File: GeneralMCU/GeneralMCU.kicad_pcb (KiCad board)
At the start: 2 copper layers, 59 parts, among them J1 ARM_JTAG_SWD, U1 STM32F303R6Tx, U2 SN65HVD230

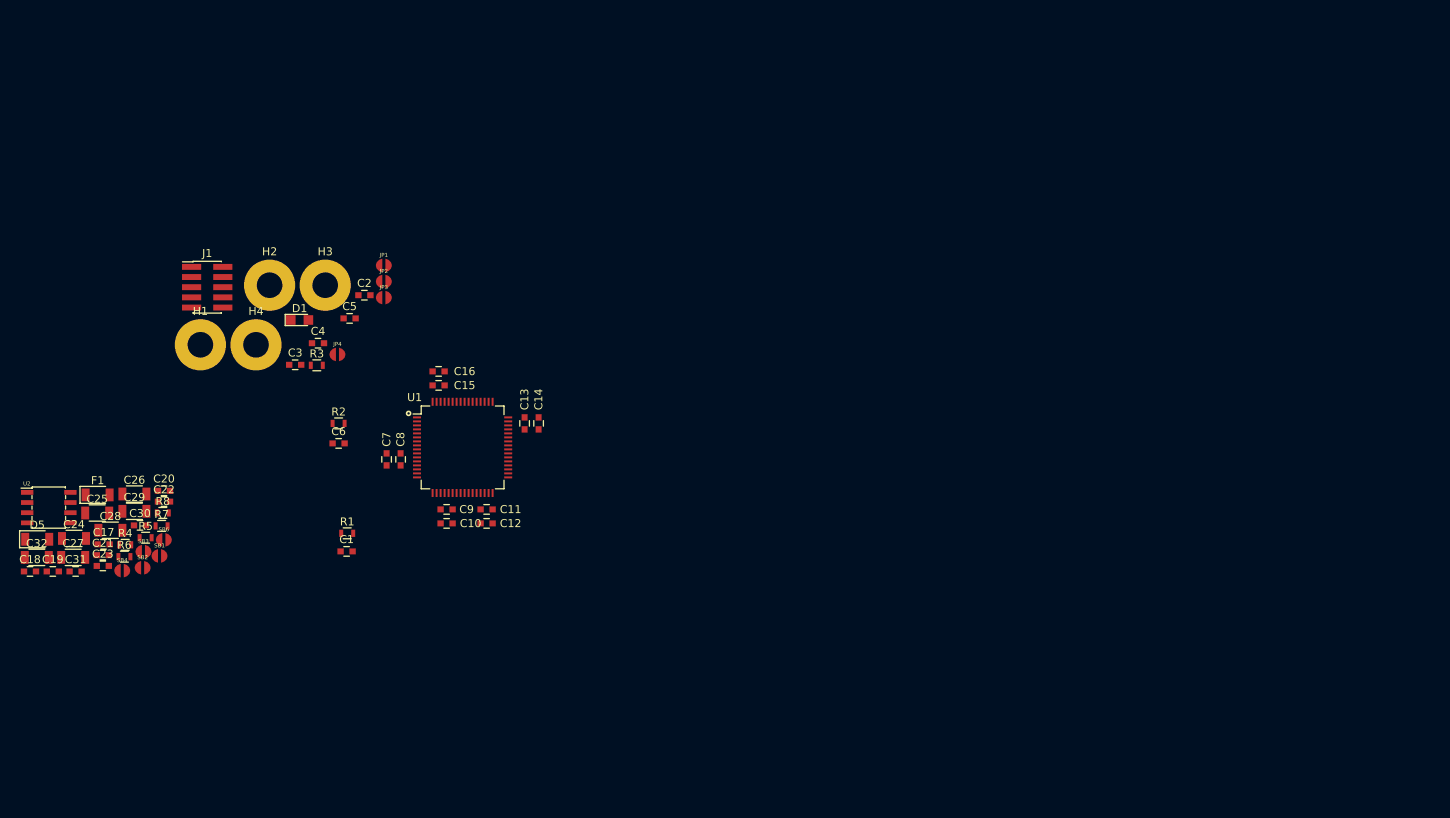
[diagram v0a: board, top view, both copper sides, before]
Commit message: Schematic getting toasty.
99% Percent of symbols added with 90% of footprints filled in, 30% of parts spec'd.

Layout organized by functional group
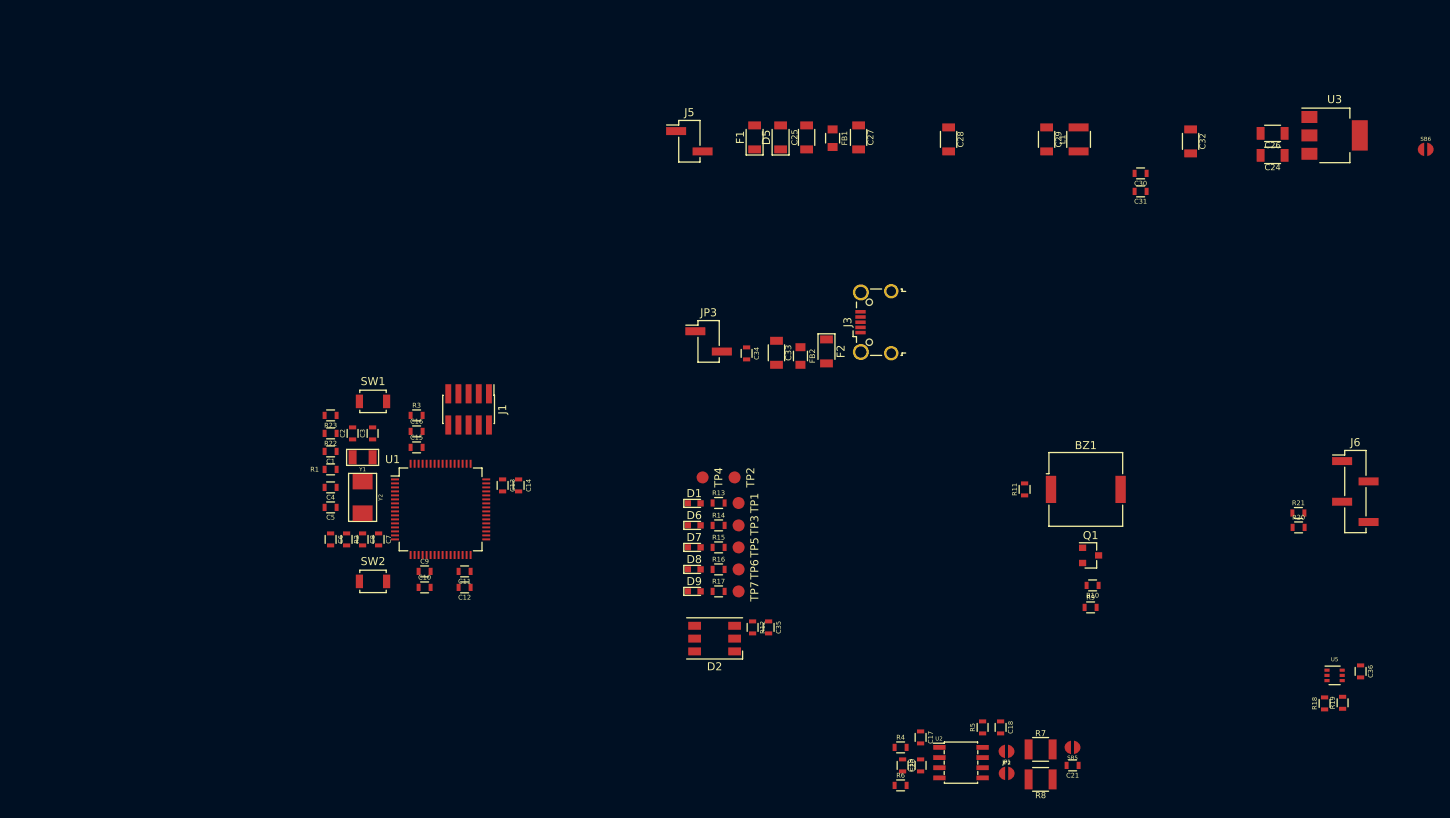
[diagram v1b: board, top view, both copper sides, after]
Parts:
- removed C22, C23: 0.1u, Capacitors_SMD:C_0603
- removed H1, H2, H3, H4: M3, MountingHole:MountingHole_3.2mm_M3_Pad
- removed JP4, SB1, SB2, SB3, SB4: Jumper_NC_Small, µ104KiCAD:JUMPER_EGG
- added BZ1: Buzzer, Buzzer_Beeper:Buzzer_Murata_PKMCS0909E4000-R1, F.Cu at (158.7, 127.8)
- added C33: 10u, µ104KiCAD_RLC:SMD_pkg_1206, F.Cu at (120.0, 110.7)
- added C34: 1u, µ104KiCAD_RLC:SMD_pkg_0603, F.Cu at (116.2, 110.8)
- added C35: 1u, µ104KiCAD_RLC:SMD_pkg_0603, F.Cu at (119.0, 145.0)
- added C36: 0.1u, µ104KiCAD_RLC:SMD_pkg_0603, F.Cu at (193.0, 150.5)
- added D2: WS2812B, LEDs:LED_WS2812-PLCC6, F.Cu at (112.2, 146.4)
- added D6: 5V, LEDs:LED_0603, F.Cu at (109.7, 132.2)
- added D7: +V, LEDs:LED_0603, F.Cu at (109.7, 135.0)
- added D8: USB, LEDs:LED_0603, F.Cu at (109.7, 137.8)
- added D9: ISO5, LEDs:LED_0603, F.Cu at (109.7, 140.5)
- added F2: 500mA PTC, Diodes_SMD:D_1206, F.Cu at (126.2, 110.5)
- added FB1: FB, µ104KiCAD_RLC:SMD_pkg_0805, F.Cu at (127.0, 83.8)
- added FB2: FB, µ104KiCAD_RLC:SMD_pkg_0805, F.Cu at (123.0, 111.1)
- added J3: USB_B_Micro, Connectors_USB:USB_Micro-B_Wuerth-629105150521_CircularHoles, F.Cu at (132.4, 106.9)
- added J5: PWR, Pin_Headers:Pin_Header_Straight_1x02_Pitch2.54mm_SMD_Pin1Left, F.Cu at (109.1, 84.2)
- added J6: OLED, Pin_Headers:Pin_Header_Straight_1x04_Pitch2.54mm_SMD_Pin1Left, F.Cu at (192.3, 128.0)
- added L1: 22u, µ104KiCAD_RLC:SMD_pkg_1210, F.Cu at (157.8, 84.0)
- added Q1: Q_NMOS_DGS, TO_SOT_Packages_SMD:SOT-23, F.Cu at (159.2, 136.0)
- added R10: 1k, µ104KiCAD_RLC:SMD_pkg_0603, F.Cu at (159.5, 139.8)
- added R11: 0, µ104KiCAD_RLC:SMD_pkg_0603, F.Cu at (151.0, 127.8)
- added R12: 10k, µ104KiCAD_RLC:SMD_pkg_0603, F.Cu at (117.0, 145.0)
- added R13: 10k, µ104KiCAD_RLC:SMD_pkg_0603, F.Cu at (112.8, 129.4)
- added R14: 10k, µ104KiCAD_RLC:SMD_pkg_0603, F.Cu at (112.8, 132.2)
- added R15: 10k, µ104KiCAD_RLC:SMD_pkg_0603, F.Cu at (112.8, 135.0)
- added R16: 10k, µ104KiCAD_RLC:SMD_pkg_0603, F.Cu at (112.8, 137.8)
- added R17: 10k, µ104KiCAD_RLC:SMD_pkg_0603, F.Cu at (112.8, 140.5)
- added R18: 0, µ104KiCAD_RLC:SMD_pkg_0603, F.Cu at (188.5, 154.5)
- added R19: 0, µ104KiCAD_RLC:SMD_pkg_0603, F.Cu at (190.8, 154.4)
- added R20: 0, µ104KiCAD_RLC:SMD_pkg_0603, F.Cu at (185.2, 132.5)
- added R21: 0, µ104KiCAD_RLC:SMD_pkg_0603, F.Cu at (185.2, 130.7)
- added R22: 4.7k, µ104KiCAD_RLC:SMD_pkg_0603, F.Cu at (64.2, 120.8)
- added R23: 4.7k, µ104KiCAD_RLC:SMD_pkg_0603, F.Cu at (64.2, 118.5)
- added R9: 1k, µ104KiCAD_RLC:SMD_pkg_0603, F.Cu at (159.2, 142.5)
- added SB5: Jumper_NC_Small, µ104KiCAD:JUMPER_EGG, F.Cu at (157.0, 160.0)
- added SW1: USER, Buttons_Switches_SMD:SW_SPST_B3U-1000P, F.Cu at (69.5, 116.8)
- added SW2: RESET, Buttons_Switches_SMD:SW_SPST_B3U-1000P, F.Cu at (69.5, 139.2)
- added TP1: 3V3, Measurement_Points:Measurement_Point_Round-SMD-Pad_Small, F.Cu at (115.2, 129.4)
- added TP2: GND, Measurement_Points:Measurement_Point_Round-SMD-Pad_Small, F.Cu at (114.8, 126.2)
- added TP3: 5V, Measurement_Points:Measurement_Point_Round-SMD-Pad_Small, F.Cu at (115.2, 132.2)
- added TP4: ISOGND, Measurement_Points:Measurement_Point_Round-SMD-Pad_Small, F.Cu at (110.8, 126.2)
- added TP5: +V, Measurement_Points:Measurement_Point_Round-SMD-Pad_Small, F.Cu at (115.2, 135.0)
- added TP6: USB, Measurement_Points:Measurement_Point_Round-SMD-Pad_Small, F.Cu at (115.2, 137.8)
- added TP7: 5V ISO, Measurement_Points:Measurement_Point_Round-SMD-Pad_Small, F.Cu at (115.2, 140.5)
- added U3: AZ1117-3.3, TO_SOT_Packages_SMD:SOT-223-3_TabPin2, F.Cu at (189.8, 83.5)
- added U5: BME280, µ104KiCAD_IC:SOT-363-6, F.Cu at (189.8, 151.0)
- added Y1: 32.768kHz, µ104KiCAD_IC:Crystal_NDK_NX3215SA, F.Cu at (68.2, 123.8)
- added Y2: 8MHz, µ104KiCAD_IC:Crystal_L5_W3.2, F.Cu at (68.2, 128.8)
- C1, C10, C11, C12, C13, C14, C15, C16, C17, C18, C19, C2, C20, C21, C3, C30, C31, C4, C5, C6, C7, C8, C9: footprint Capacitors_SMD:C_0603 -> µ104KiCAD_RLC:SMD_pkg_0603
- C24, C25, C26, C27, C29, C32: footprint Capacitors_SMD:C_1206 -> µ104KiCAD_RLC:SMD_pkg_1206
- C28: value 10u -> 22u; footprint Capacitors_SMD:C_1206 -> µ104KiCAD_RLC:SMD_pkg_1206
- D1: value LED -> 3V3; footprint LEDs:LED_0805 -> LEDs:LED_0603
- JP3: footprint µ104KiCAD:JUMPER_EGG -> Pin_Headers:Pin_Header_Straight_1x02_Pitch2.54mm_SMD_Pin1Left
- R1, R2, R3, R4, R5, R6: footprint Resistors_SMD:R_0603 -> µ104KiCAD_RLC:SMD_pkg_0603
- R7, R8: footprint Resistors_SMD:R_0603 -> µ104KiCAD_RLC:SMD_pkg_1210
- moved SB6 165.1 mm to (201.1, 85.2)
- moved C24 157.3 mm to (182.0, 86.0), turned to 180 degrees
- moved C32 153.3 mm to (171.8, 84.2), turned to 270 degrees
- moved C26 149.2 mm to (182.0, 83.2), turned to 180 degrees
- moved C31 141.3 mm to (165.5, 90.5), turned to 180 degrees
- moved C30 132.6 mm to (165.5, 88.2), turned to 180 degrees
- moved C21 124.0 mm to (157.0, 162.2), turned to 180 degrees
- moved C29 123.1 mm to (153.8, 84.0), turned to 270 degrees
- moved C18 122.9 mm to (148.0, 157.5), turned to 270 degrees
- moved U2 118.4 mm to (143.1, 161.9)
- moved C28 115.6 mm to (141.5, 84.0), turned to 270 degrees
- moved R8 114.7 mm to (153.0, 164.0), turned to 180 degrees
- moved R7 113.4 mm to (153.0, 160.2)
- moved C27 111.3 mm to (130.2, 83.8), turned to 270 degrees
- moved C19 111.2 mm to (138.0, 162.2), turned to 90 degrees
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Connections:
- D1 pad 1: Net-(D1-Pad1) -> GND
- J1 pad 1: Net-(J1-Pad1) -> +3V3
- J1 pad 3: Net-(J1-Pad3) -> GND
- J1 pad 5: Net-(J1-Pad3) -> GND
- J1 pad 9: Net-(J1-Pad9) -> GND
- JP3 pad 1: CHASSIS -> VBUS
- JP3 pad 2: Net-(H3-Pad1) -> +5V
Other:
- board text added: "Fix Soldermask for imbetween pins - Gammel's video"

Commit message: Needs castellated pads and sch review
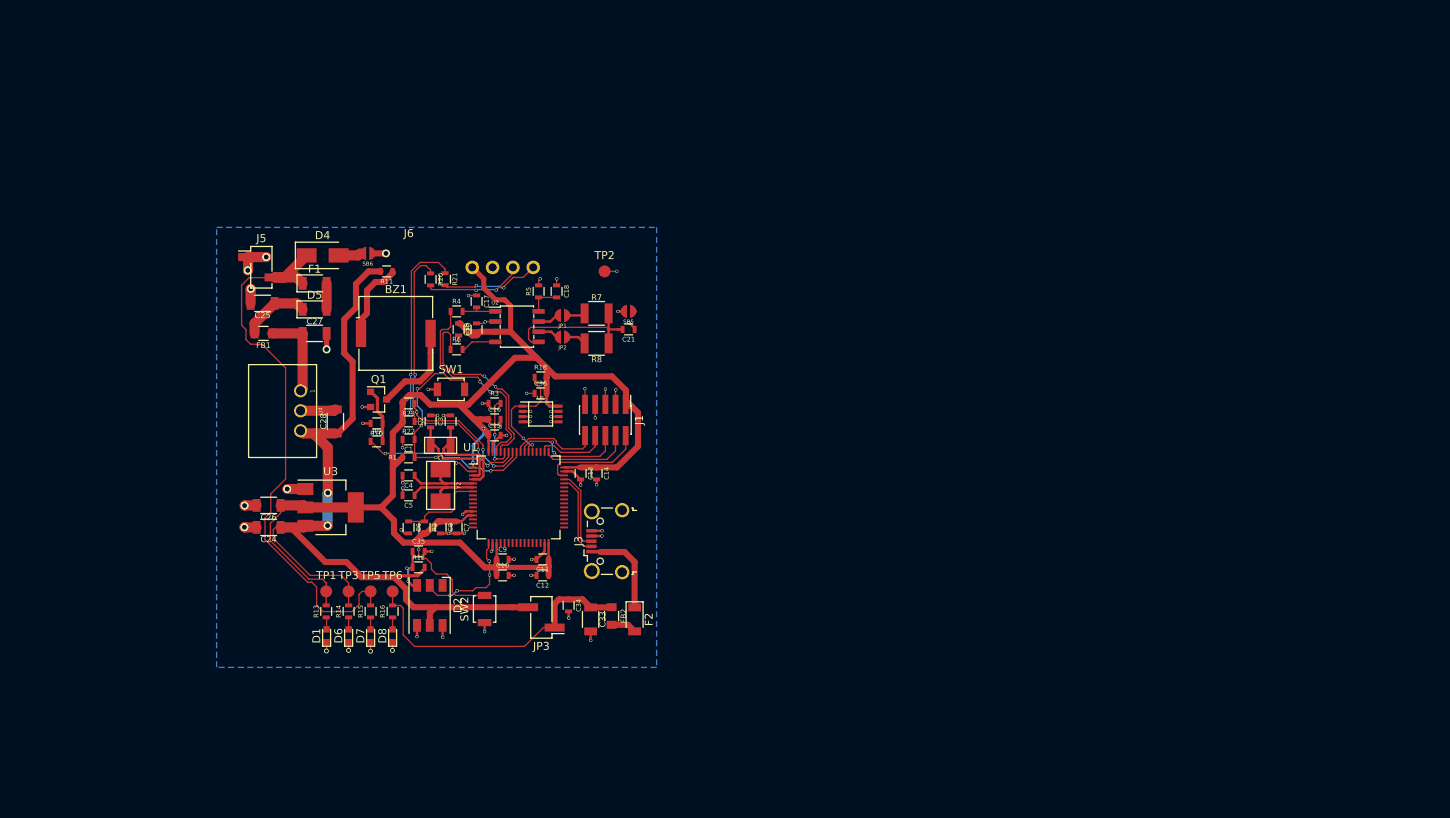
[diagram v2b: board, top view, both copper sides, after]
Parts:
- removed C29, C32: 10u, µ104KiCAD_RLC:SMD_pkg_1206
- removed C30, C31: 330p, µ104KiCAD_RLC:SMD_pkg_0603
- removed D9: ISO5, LEDs:LED_0603
- removed L1: 22u, µ104KiCAD_RLC:SMD_pkg_1210
- removed R17: 10k, µ104KiCAD_RLC:SMD_pkg_0603
- removed R19: 0, µ104KiCAD_RLC:SMD_pkg_0603
- removed TP4: ISOGND, Measurement_Points:Measurement_Point_Round-SMD-Pad_Small
- removed TP7: 5V ISO, Measurement_Points:Measurement_Point_Round-SMD-Pad_Small
- added D4: D_TVS, Diodes_SMD:D_SMA, F.Cu at (63.2, 98.5)
- added U4: P78E05-1000, µ104KiCAD_DCDC:Recom_INNOLINE-R-78E, F.Cu at (60.5, 118.0)
- J6: footprint Pin_Headers:Pin_Header_Straight_1x04_Pitch2.54mm_SMD_Pin1Left -> µ104KiCAD:I2C_OLED
- R18: value 0 -> 4.7k
- U5: value BME280 -> DS18B20; footprint µ104KiCAD_IC:SOT-363-6 -> µ104KiCAD_IC:MSOP-8
- moved C24 133.8 mm to (56.5, 132.5)
- moved C26 133.8 mm to (56.5, 129.8)
- moved U3 133.8 mm to (64.2, 130.0)
- moved SB6 132.9 mm to (68.9, 98.2), turned to 180 degrees
- moved R20 112.8 mm to (76.8, 101.5), turned to 270 degrees
- moved R21 110.6 mm to (78.5, 101.5), turned to 270 degrees
- moved C36 108.2 mm to (90.5, 115.8), turned to 0 degrees
- moved J6 107.5 mm to (85.5, 116.0)
- moved R18 106.1 mm to (90.5, 113.8), turned to 0 degrees
- moved U5 104.5 mm to (90.5, 118.3)
- moved R10 91.8 mm to (70.0, 119.5)
- moved R9 91.6 mm to (70.0, 121.8)
- moved Q1 91.1 mm to (70.2, 116.5)
- moved BZ1 88.4 mm to (72.4, 108.2)
- moved C28 84.4 mm to (64.8, 119.2), turned to 90 degrees
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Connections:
- net /PA11 renamed /USB_DM
- net /PA12 renamed /USB_DP
- C36 pad 1: +3V3 -> GND
- C36 pad 2: GND -> +3V3
- D2 pad 2: /USR_LED -> /PA3
- R18 pad 1: /I2C1_SDA -> /PD2
- R18 pad 2: Net-(R18-Pad2) -> +3V3
- U1 pad 57: /PB5 -> /BUZZ
- U5 pad 1: GND -> /PD2
- U5 pad 2: +3V3 -> Net-(U5-Pad2)
- U5 pad 3: Net-(R18-Pad2) -> Net-(U5-Pad3)
- U5 pad 4: Net-(R19-Pad2) -> GND
- U5 pad 5: GND -> Net-(U5-Pad5)
- U5 pad 6: +3V3 -> Net-(U5-Pad6)
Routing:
- net +3V3: track 0.00 -> 183.4 mm, vias 0 -> 2
- net +5V: track 0.00 -> 106.7 mm, vias 0 -> 2
- net GND: track 0.00 -> 76.0 mm, vias 0 -> 52
- net +V: track 0.00 -> 71.2 mm
- net /I2C1_SDA: track 0.00 -> 40.6 mm, vias 0 -> 4
- net /I2C1_SCL: track 0.00 -> 39.0 mm, vias 0 -> 4
- net VBUS: track 0.00 -> 37.8 mm
- net /NRST: track 0.00 -> 27.5 mm, vias 0 -> 2
- net /CAN_TX: track 0.00 -> 25.9 mm, vias 0 -> 2
- net /PC13: track 0.00 -> 25.4 mm, vias 0 -> 4
- net /CAN_RX: track 0.00 -> 25.0 mm, vias 0 -> 2
- net /BUZZ: track 0.00 -> 21.2 mm, vias 0 -> 2
- net /Vref: track 0.00 -> 19.1 mm
- net /JTAG_JTDO: track 0.00 -> 14.6 mm, vias 0 -> 2
- net /PD2: track 0.00 -> 14.3 mm, vias 0 -> 2
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- added copper zone on B.Cu, net GND
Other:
- net class Default: clearance 0.2 -> 0.17
- rule pad_to_mask_clearance: 0.051 -> 0.0254
- rule solder_mask_min_width: 0.25 -> 0.127
- rule trace_clearance: 0.2 -> 0.17
- rule trace_min: 0.2 -> 0.1524
- board text removed: "Fix Soldermask for imbetween pins - Gammel's video"

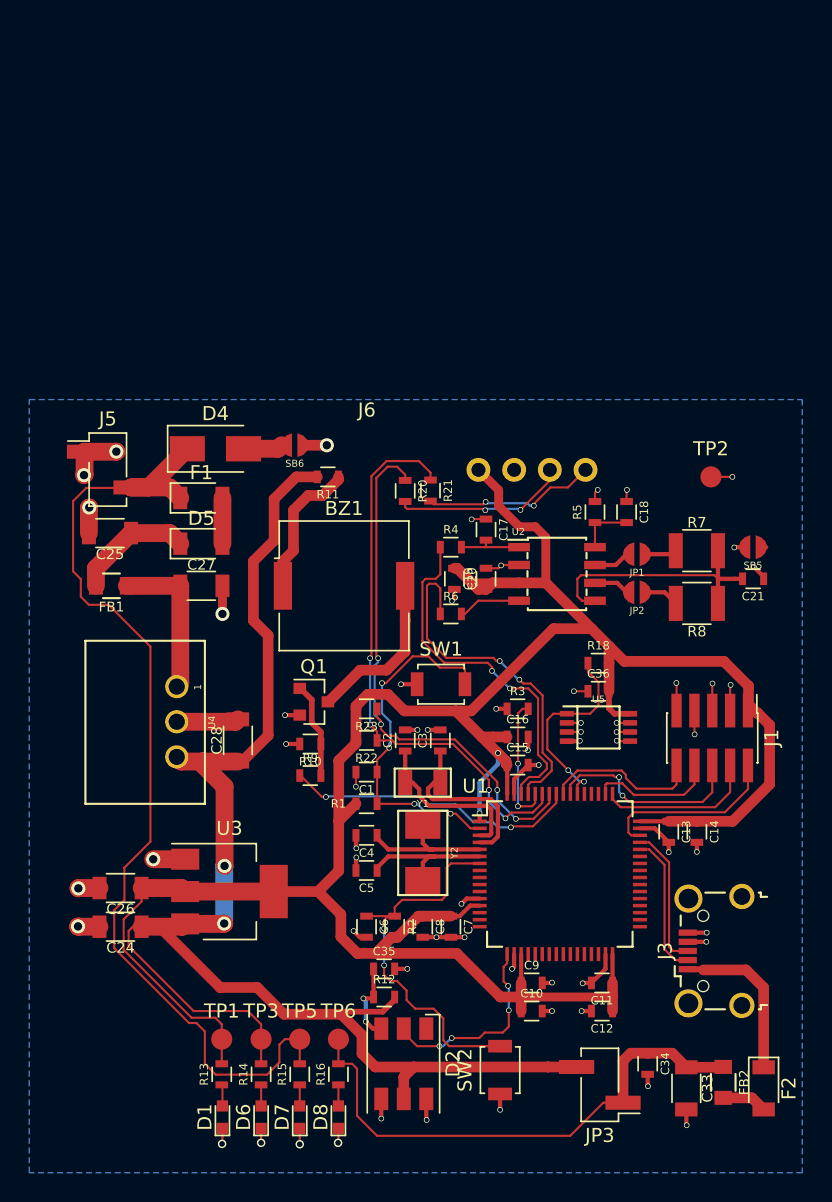
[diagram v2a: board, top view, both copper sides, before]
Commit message: Redid the layout of the board to be better
Smaller 30x80mm footprint. Sch symbol and footprint for the board can be found under the example folder. Routing needs to be made nice yet.
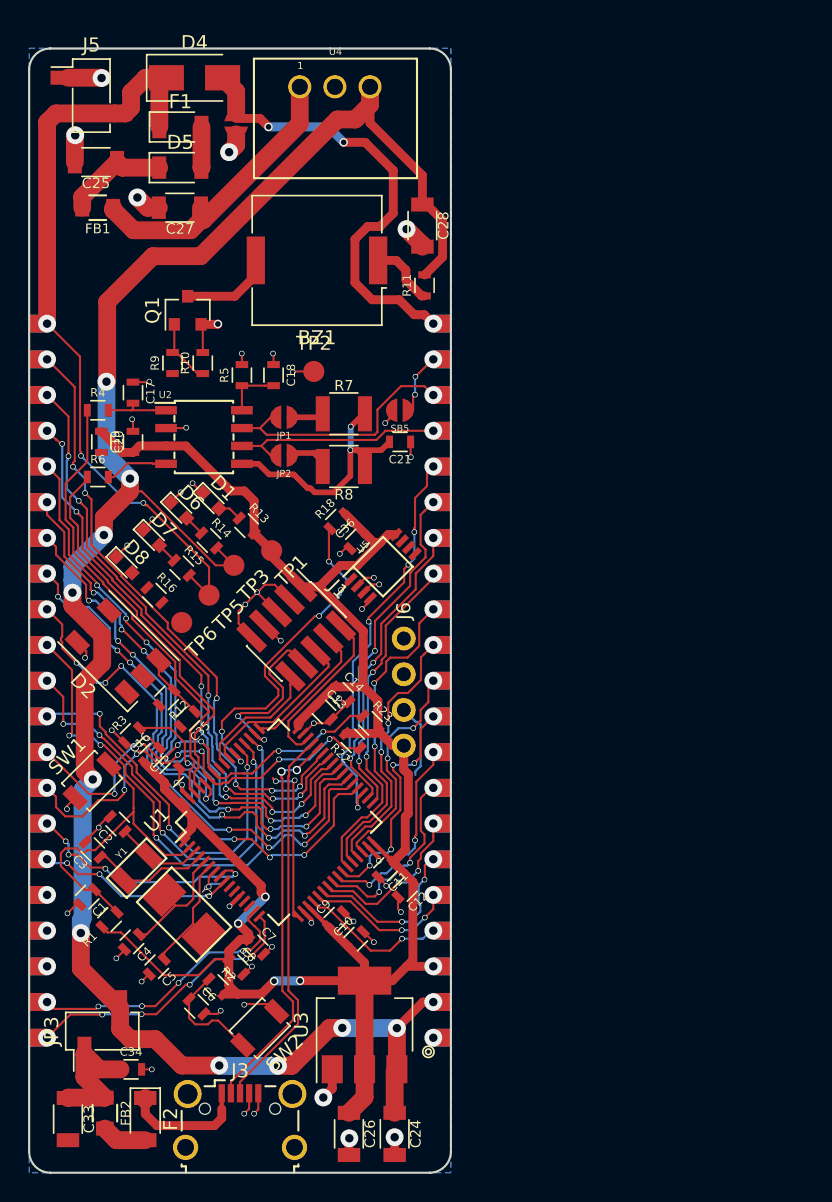
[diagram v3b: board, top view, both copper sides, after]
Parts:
- removed R20, R21: 0, µ104KiCAD_RLC:SMD_pkg_0603
- added J2: SMD castellation PKG, µ104KiCAD:PAD42, F.Cu at (65.0, 115.0)
- Q1: footprint TO_SOT_Packages_SMD:SOT-23 -> Package_TO_SOT_SMD:SOT-23
- moved U4 46.6 mm to (71.8, 72.8), turned to 0 degrees
- moved C33 44.0 mm to (52.8, 146.2)
- moved F2 44.0 mm to (58.3, 146.2)
- moved FB2 44.0 mm to (55.4, 145.8)
- moved D1 43.9 mm to (62.9, 102.2), turned to 315 degrees
- moved D6 43.6 mm to (60.6, 102.9), turned to 315 degrees
- moved D7 42.6 mm to (58.7, 104.8), turned to 315 degrees
- moved D8 42.1 mm to (56.8, 106.8), turned to 315 degrees
- moved R13 39.1 mm to (65.5, 104.0), turned to 315 degrees
- moved C28 38.9 mm to (78.0, 82.6), turned to 270 degrees
- moved R14 38.2 mm to (62.8, 105.0), turned to 315 degrees
- moved R15 37.0 mm to (60.9, 107.0), turned to 315 degrees
- moved C34 36.8 mm to (57.2, 142.7), turned to 0 degrees
- moved R16 36.5 mm to (58.9, 108.9), turned to 315 degrees
- moved J3 35.8 mm to (65.0, 146.2), turned to 0 degrees
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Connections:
- net /PA3 renamed /USR_LED
- J6 pad 3: Net-(J6-Pad3) -> /I2C1_SCL
- J6 pad 4: Net-(J6-Pad4) -> /I2C1_SDA
- U1 pad 8: Net-(U1-Pad8) -> /PC0
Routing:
- net /PA10: track 0.00 -> 44.0 mm, vias 0 -> 7
- net /PC9: track 0.00 -> 43.1 mm, vias 0 -> 7
- net /PA9: track 0.00 -> 42.6 mm, vias 0 -> 7
- net /PC8: track 0.00 -> 42.4 mm, vias 0 -> 7
- net /PA8: track 0.00 -> 41.8 mm, vias 0 -> 7
- net /PC7: track 0.00 -> 41.0 mm, vias 0 -> 7
- net +3V3: track 183.4 -> 143.2 mm, vias 2 -> 5
- net /PC6: track 0.00 -> 38.7 mm, vias 0 -> 7
- net /PB15: track 0.00 -> 38.5 mm, vias 0 -> 7
- net /PC10: track 0.00 -> 35.3 mm, vias 0 -> 5
- net +5V: track 106.7 -> 141.3 mm, vias 2 -> 11
- net /PC11: track 0.00 -> 30.5 mm, vias 0 -> 5
- net CHASSIS: track 3.35 -> 32.6 mm, vias 0 -> 3
- net /PB14: track 0.00 -> 28.7 mm, vias 0 -> 5
- net VBUS: track 37.8 -> 9.33 mm
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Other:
- board outline added: 30 x 80 mm
- board text added: "R = 1.5mm Corners"
